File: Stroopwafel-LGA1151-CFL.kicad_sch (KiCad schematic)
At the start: 0 parts

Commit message: Added pcie slot and cpu clocks
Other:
- added sheet PCIe_slots (PCIe_slots.kicad_sch)
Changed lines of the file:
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@@
+	)
+	(sheet
+		(at 76.2 127)
+		(size 38.1 38.1)
+		(exclude_from_sim no)
+		(in_bom yes)
+		(on_board yes)
+		(dnp no)
+		(fields_autoplaced yes)
+		(stroke
+			(width 0.1524)
+			(type solid)
+		)
+		(fill
+			(color 0 0 0 0.0000)
+		)
+		(property "Sheetname" "PCIe_slots"
+			(at 76.2 126.2884 0)
+			(effects
+				(font
+					(size 1.27 1.27)
+				)
+				(justify left bottom)
+			)
+		)
+		(property "Sheetfile" "PCIe_slots.kicad_sch"
+			(at 76.2 165.6846 0)
+			(effects
+				(font
+					(size 1.27 1.27)
+				)
+				(justify left top)
+			)
+		)
+		(instances
+			(project "Stroopwafel-LGA1151-CFL"
+				(path "/4bc771b8-eb19-46d0-8798-27231a7c6e83"
+					(page "13")
+				)
+			)
+		)
 	)
 	(sheet

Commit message: Some DP and power work
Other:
- added sheet Display_ports (Display_ports.kicad_sch)
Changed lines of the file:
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@@
+	)
+	(sheet
+		(at 127 127)
+		(size 38.1 38.1)
+		(exclude_from_sim no)
+		(in_bom yes)
+		(on_board yes)
+		(dnp no)
+		(fields_autoplaced yes)
+		(stroke
+			(width 0.1524)
+			(type solid)
+		)
+		(fill
+			(color 0 0 0 0.0000)
+		)
+		(property "Sheetname" "Display_ports"
+			(at 127 126.2884 0)
+			(effects
+				(font
+					(size 1.27 1.27)
+				)
+				(justify left bottom)
+			)
+		)
+		(property "Sheetfile" "Display_ports.kicad_sch"
+			(at 127 165.6846 0)
+			(effects
+				(font
+					(size 1.27 1.27)
+				)
+				(justify left top)
+			)
+		)
+		(instances
+			(project "Stroopwafel-LGA1151-CFL"
+				(path "/4bc771b8-eb19-46d0-8798-27231a7c6e83"
+					(page "14")
+				)
+			)
+		)
 	)
 	(sheet

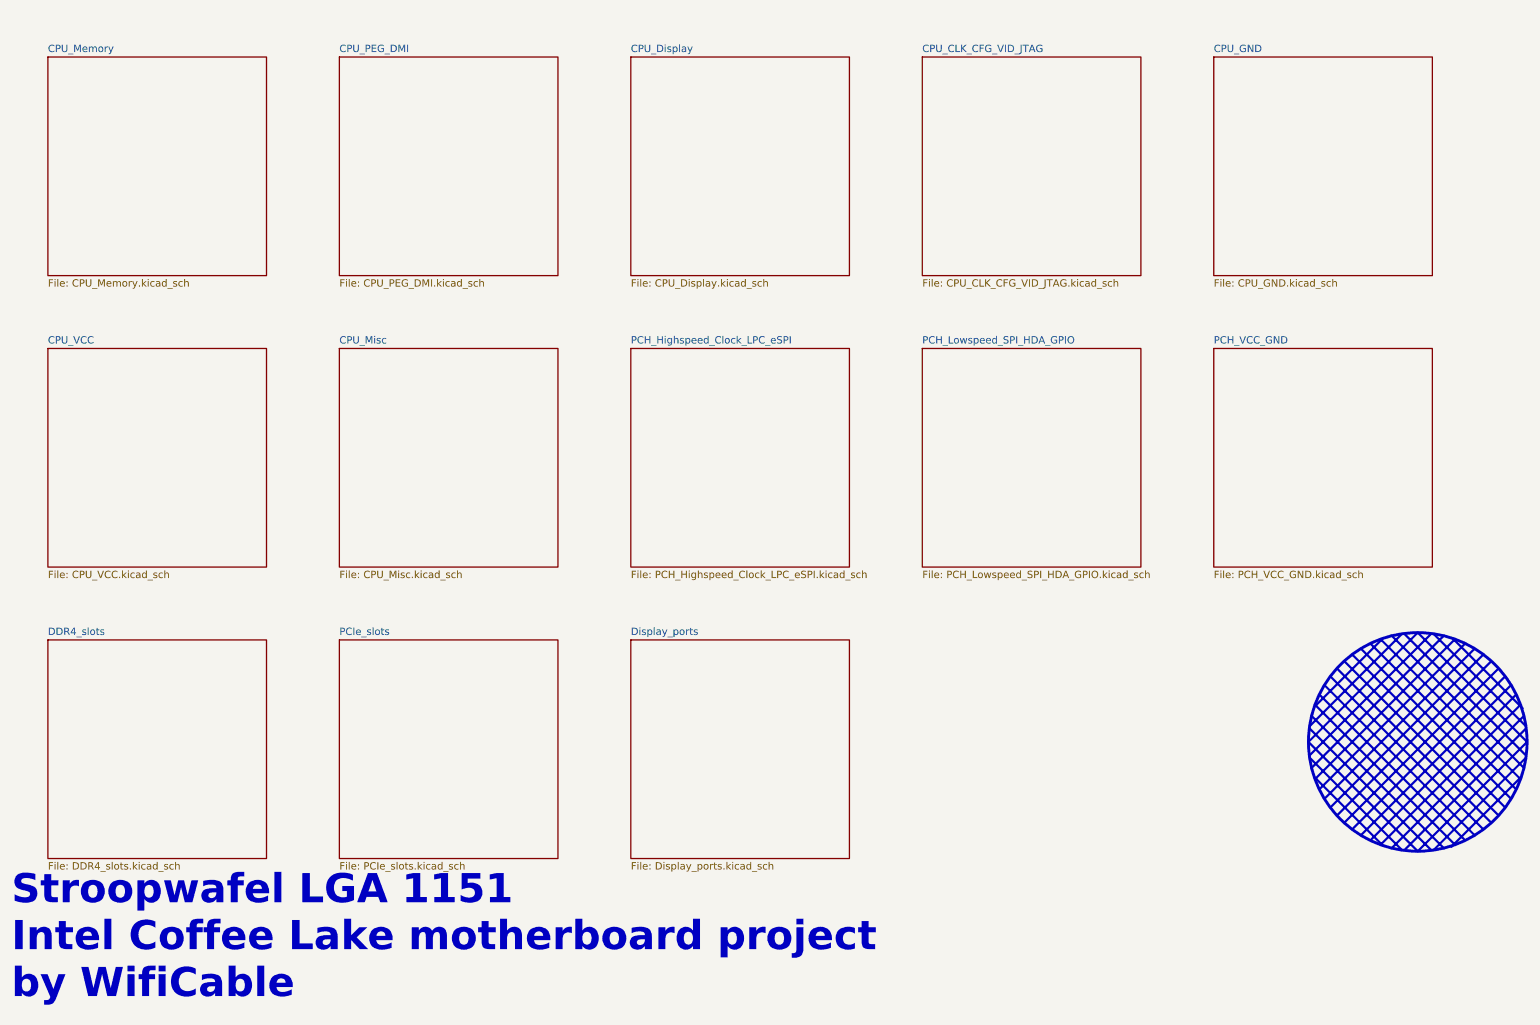
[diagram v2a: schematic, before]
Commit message: Made a cool table of contents on the root schematic page
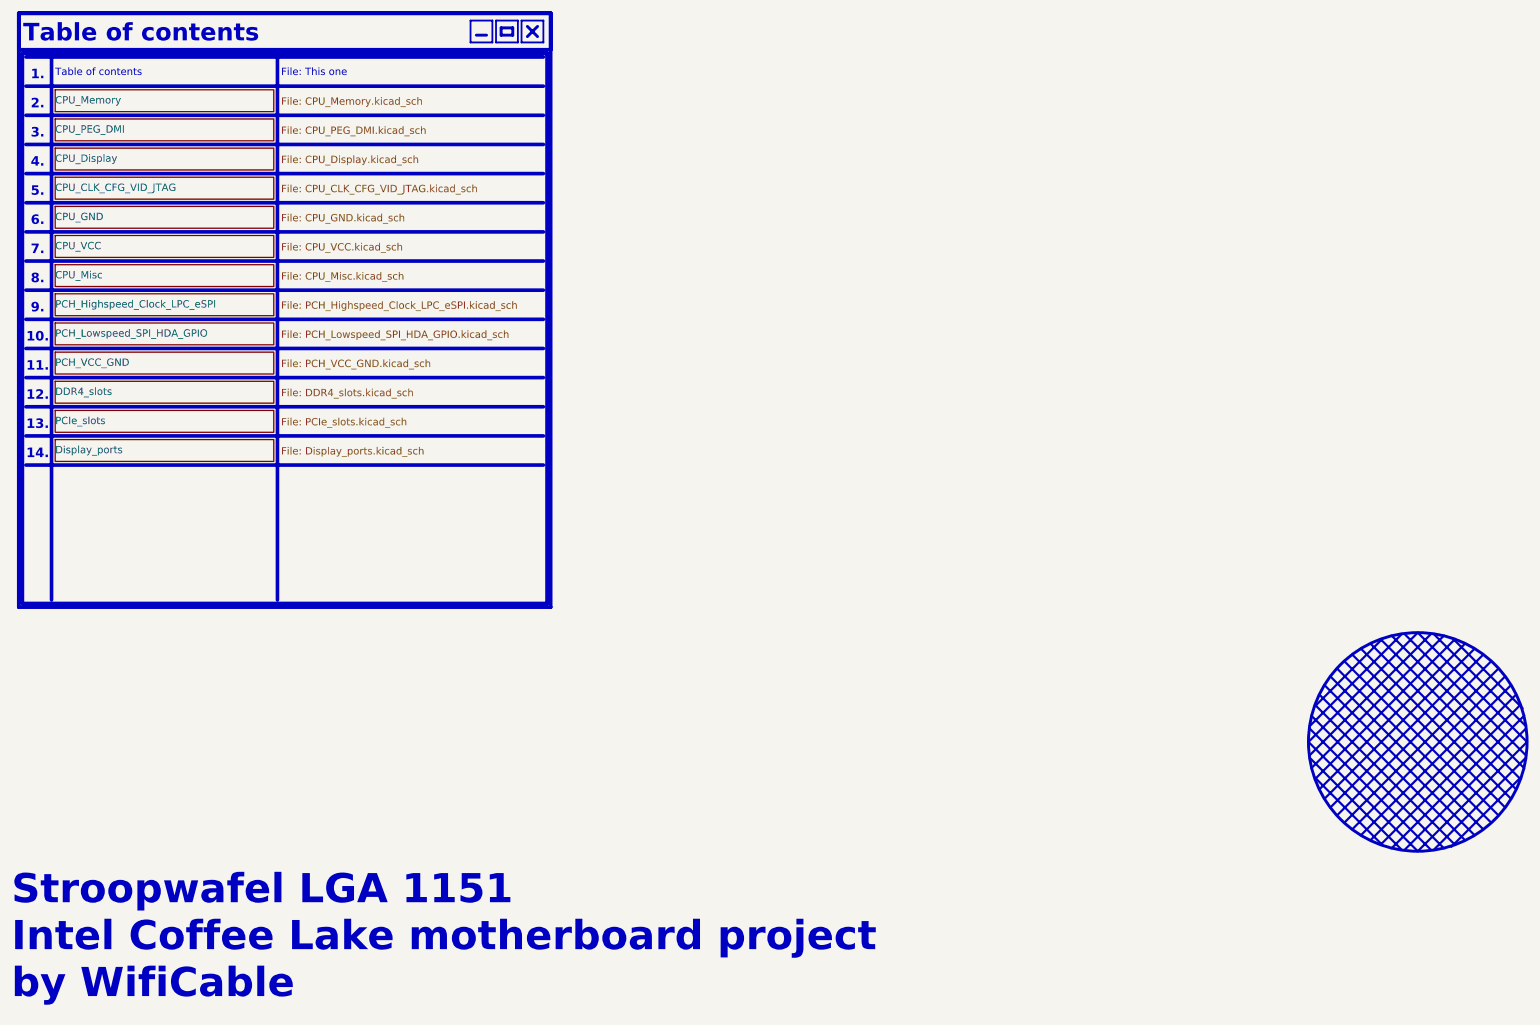
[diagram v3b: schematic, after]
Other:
- note added: "1."
- note added: "10."
- note added: "11."
- note added: "12."
- note added: "13."
- note added: "14."
- note added: "2."
- note added: "3."
- note added: "4."
- note added: "5."
- note added: "6."
- note added: "7."
- note added: "8."
- note added: "9."
- note added: "File: This one"
- note added: "Table of contents"
